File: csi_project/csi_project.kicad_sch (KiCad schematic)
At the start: 26 parts, among them U2 CSI080

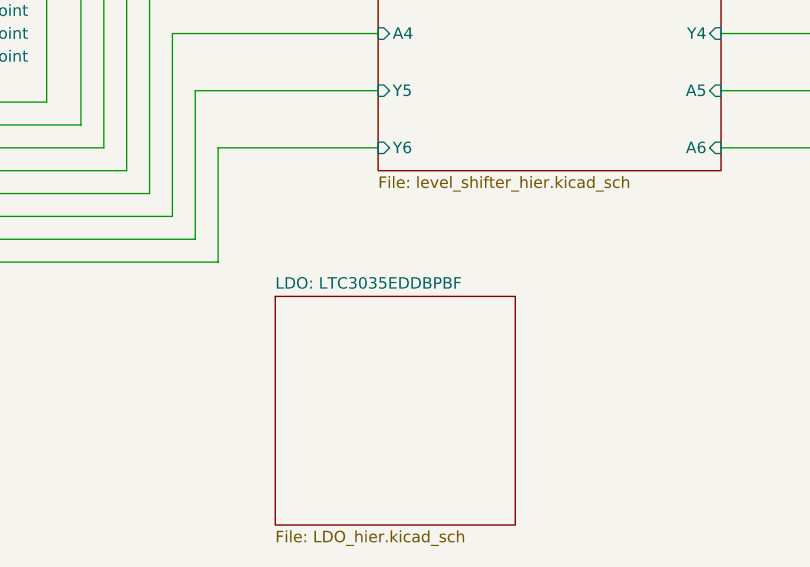
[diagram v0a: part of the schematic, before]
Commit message: Changed file name of schematic pdf, causing git cloning issues.
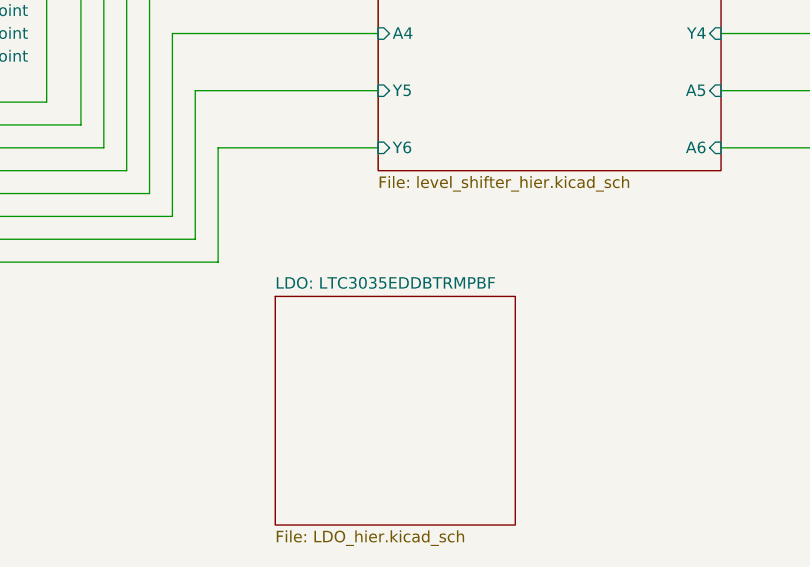
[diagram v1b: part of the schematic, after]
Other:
- sheet LDO: LTC3035EDDBPBF renamed LDO: LTC3035EDDBTRMPBF
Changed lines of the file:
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@@
 			(color 0 0 0 0.0000)
 		)
-		(property "Sheetname" "LDO: LTC3035EDDBPBF"
+		(property "Sheetname" "LDO: LTC3035EDDBTRMPBF"
 			(at 149.86 121.2084 0)
 			(effects

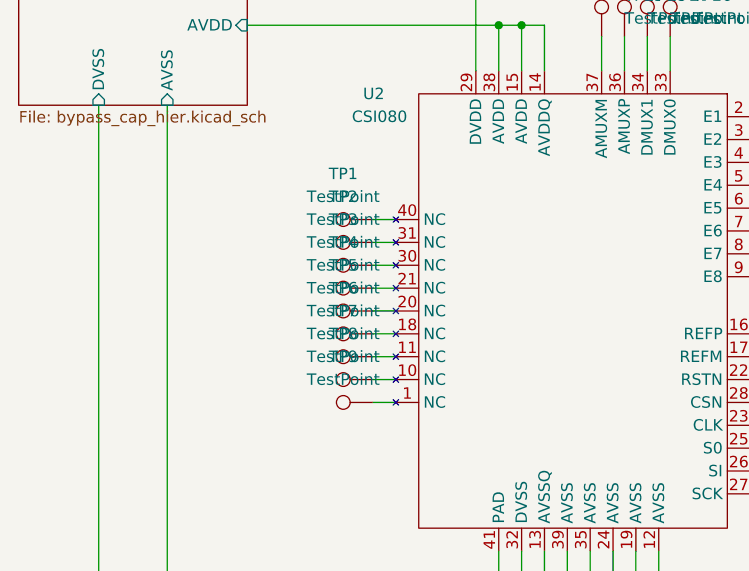
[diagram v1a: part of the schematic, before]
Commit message: Fixed issues with Footprint assignment to main components,
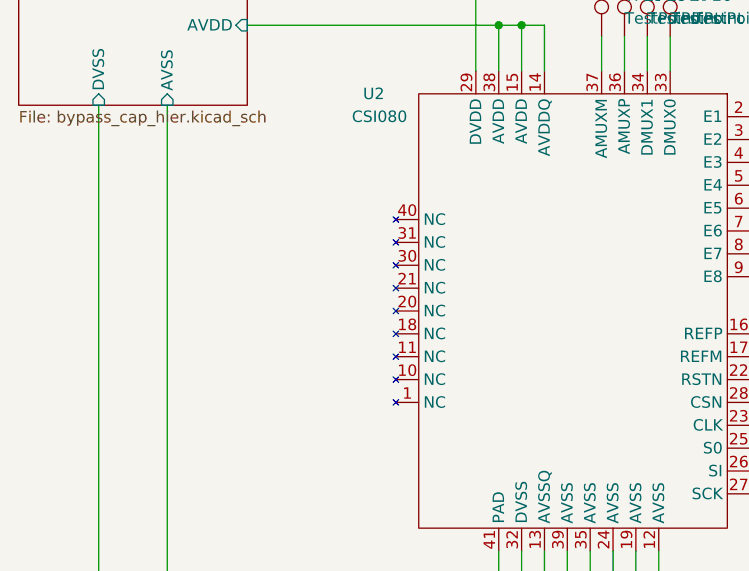
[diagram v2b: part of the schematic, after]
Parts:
- removed TP1, TP2, TP3, TP4, TP5, TP6, TP7, TP8, TP9: TestPoint, symbol Connector:TestPoint

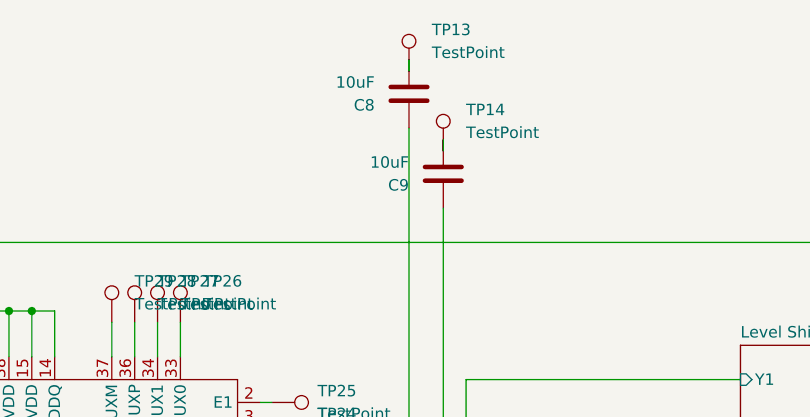
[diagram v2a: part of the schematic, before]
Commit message: Imported custom capacitor and resistor symbols and footprints, and assigned them accordingly.
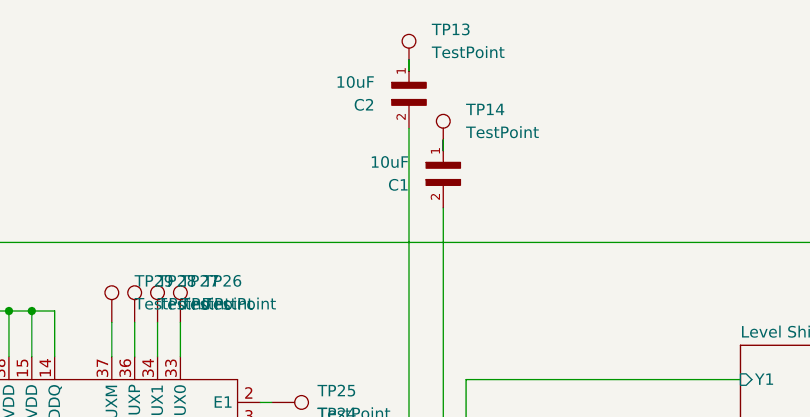
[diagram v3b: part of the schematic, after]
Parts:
- removed C8, C9: 10uF, symbol Device:C
- added C1, C2: 10uF, Custom Caps n Res:CAP_C3225X8R1E106K250AC, symbol Custom Caps n Res:C3225X8R1E106K250AC
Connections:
- net at TP14.1: now also C1.1
- net at U2.16 (REFP): now also C2.2
- net at TP13.1: now also C2.1
- net at U2.17 (REFM): now also C1.2

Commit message: Assigned footprints to testpoints
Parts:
- TP13, TP14, TP18, TP19, TP20, TP21, TP22, TP23, TP24, TP25, TP26, TP27, TP28, TP29: footprint (none) -> TestPoint:TestPoint_THTPad_4.0x4.0mm_Drill2.0mm
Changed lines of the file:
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@@
 			)
 		)
-		(property "Footprint" ""
+		(property "Footprint" "TestPoint:TestPoint_THTPad_4.0x4.0mm_Drill2.0mm"
 			(at 109.22 99.06 0)
 			(effects
@@
 			)
 		)
-		(property "Footprint" ""
+		(property "Footprint" "TestPoint:TestPoint_THTPad_4.0x4.0mm_Drill2.0mm"
 			(at 99.06 67.31 0)
 			(effects
@@
 			)
 		)
-		(property "Footprint" ""
+		(property "Footprint" "TestPoint:TestPoint_THTPad_4.0x4.0mm_Drill2.0mm"
 			(at 109.22 93.98 0)
 			(effects
@@
 			)
 		)
-		(property "Footprint" ""
+		(property "Footprint" "TestPoint:TestPoint_THTPad_4.0x4.0mm_Drill2.0mm"
 			(at 133.35 48.26 0)
 			(effects
@@
 			)
 		)
-		(property "Footprint" ""
+		(property "Footprint" "TestPoint:TestPoint_THTPad_4.0x4.0mm_Drill2.0mm"
 			(at 109.22 96.52 0)
 			(effects
@@
 			)
 		)
-		(property "Footprint" ""
+		(property "Footprint" "TestPoint:TestPoint_THTPad_4.0x4.0mm_Drill2.0mm"
 			(at 109.22 81.28 0)
 			(effects
@@
 			)
 		)
-		(property "Footprint" ""
+		(property "Footprint" "TestPoint:TestPoint_THTPad_4.0x4.0mm_Drill2.0mm"
 			(at 101.6 67.31 0)
 			(effects
@@
 			)
 		)
-		(property "Footprint" ""
+		(property "Footprint" "TestPoint:TestPoint_THTPad_4.0x4.0mm_Drill2.0mm"
 			(at 96.52 67.31 0)
 			(effects
@@
 			)
 		)
-		(property "Footprint" ""
+		(property "Footprint" "TestPoint:TestPoint_THTPad_4.0x4.0mm_Drill2.0mm"
 			(at 109.22 91.44 0)
 			(effects
@@
 			)
 		)
-		(property "Footprint" ""
+		(property "Footprint" "TestPoint:TestPoint_THTPad_4.0x4.0mm_Drill2.0mm"
 			(at 129.54 39.37 0)
 			(effects
@@
 			)
 		)
-		(property "Footprint" ""
+		(property "Footprint" "TestPoint:TestPoint_THTPad_4.0x4.0mm_Drill2.0mm"
 			(at 109.22 86.36 0)
 			(effects
@@
 			)
 		)
-		(property "Footprint" ""
+		(property "Footprint" "TestPoint:TestPoint_THTPad_4.0x4.0mm_Drill2.0mm"
 			(at 109.22 83.82 0)
 			(effects
@@
 			)
 		)
-		(property "Footprint" ""
+		(property "Footprint" "TestPoint:TestPoint_THTPad_4.0x4.0mm_Drill2.0mm"
 			(at 104.14 67.31 0)
 			(effects
@@
 			)
 		)
-		(property "Footprint" ""
+		(property "Footprint" "TestPoint:TestPoint_THTPad_4.0x4.0mm_Drill2.0mm"
 			(at 109.22 88.9 0)
 			(effects

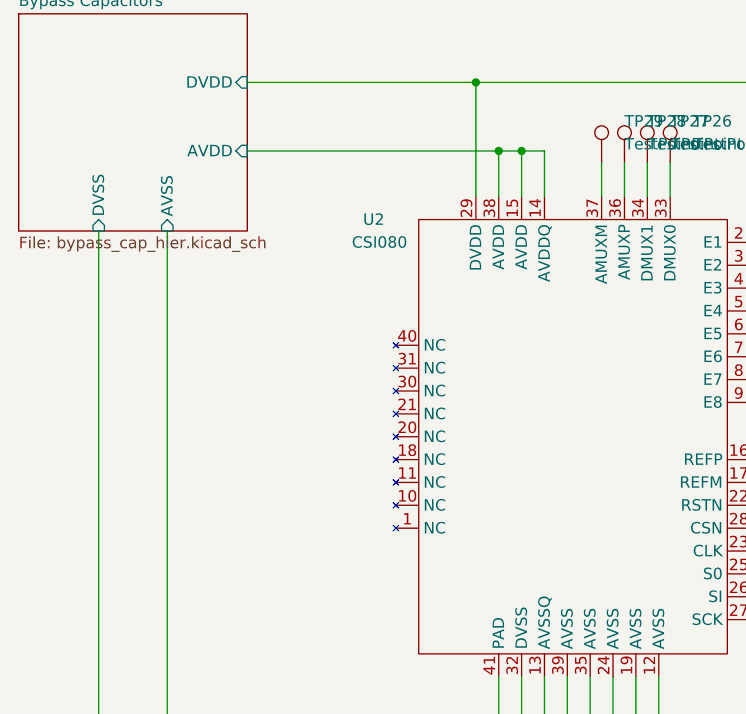
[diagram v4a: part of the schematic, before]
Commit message: Changed CSI080 symbol pins from No Connect to Bidirectional in schematic
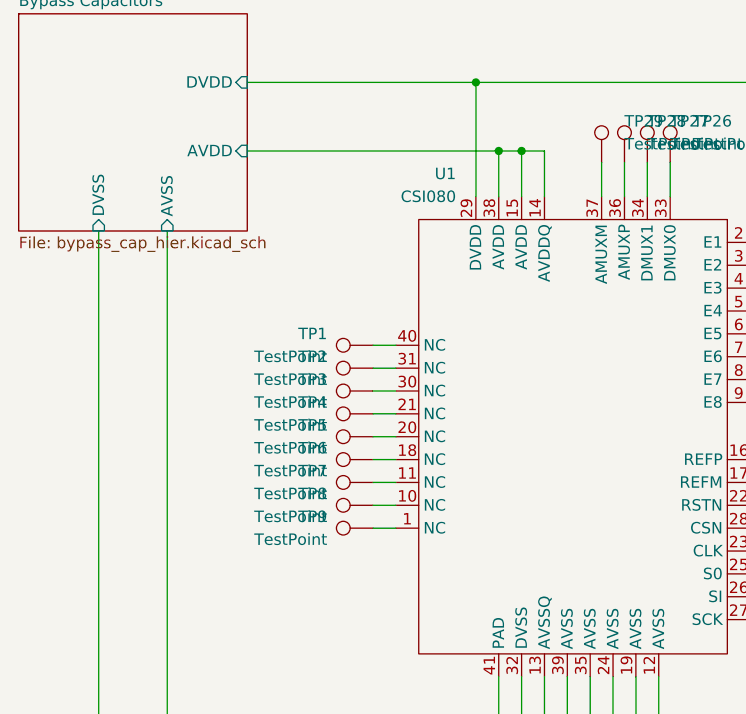
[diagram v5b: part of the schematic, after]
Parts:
- removed U2: CSI080, csi080:csi080a_MODULE, symbol csi080:CSI080_module_sorted
- added TP1, TP2, TP3, TP4, TP5, TP6, TP7, TP8, TP9: TestPoint, TestPoint:TestPoint_THTPad_4.0x4.0mm_Drill2.0mm, symbol Connector:TestPoint
- added U1: CSI080, csi080:csi080a_MODULE, symbol csi080:CSI080_module_sorted
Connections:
- net Bypass Capacitors/AVDD: now also U1.14 (AVDDQ), U1.15 (AVDD), U1.38 (AVDD)
- net Bypass Capacitors/DVDD: now also U1.29 (DVDD)
- net GND: now also U1.12 (AVSS), U1.13 (AVSSQ), U1.19 (AVSS), U1.24 (AVSS), U1.32 (DVSS), U1.35 (AVSS), U1.39 (AVSS), U1.41 (PAD)
- net Level Shifters: SN74LV1T34DBV/A4: now also U1.25 (S0)
- net Level Shifters: SN74LV1T34DBV/Y1: now also U1.22 (RSTN)
- net Level Shifters: SN74LV1T34DBV/Y2: now also U1.28 (CSN)
- net Level Shifters: SN74LV1T34DBV/Y3: now also U1.23 (CLK)
- net Level Shifters: SN74LV1T34DBV/Y5: now also U1.26 (SI)
- net Level Shifters: SN74LV1T34DBV/Y6: now also U1.27 (SCK)
- net at TP18.1: now also U1.9 (E8)
- net at TP28.1: now also U1.36 (AMUXP)
- net at C1.2: now also U1.17 (REFM)
- net at TP20.1: now also U1.7 (E6)
- net at TP19.1: now also U1.8 (E7)
- net at TP25.1: now also U1.2 (E1)
- net at TP27.1: now also U1.34 (DMUX1)
- net at C2.2: now also U1.16 (REFP)
- net at TP29.1: now also U1.37 (AMUXM)
- net at TP21.1: now also U1.6 (E5)
- net at TP24.1: now also U1.3 (E2)
- net at TP26.1: now also U1.33 (DMUX0)
- net at TP23.1: now also U1.4 (E3)
- net at TP22.1: now also U1.5 (E4)
- new net: TP8.1, U1.10 (NC)
- new net: TP9.1, U1.1 (NC)
- new net: TP7.1, U1.11 (NC)
- new net: TP6.1, U1.18 (NC)
- new net: TP5.1, U1.20 (NC)
- new net: TP4.1, U1.21 (NC)
- new net: TP3.1, U1.30 (NC)
- new net: TP2.1, U1.31 (NC)
- new net: TP1.1, U1.40 (NC)
